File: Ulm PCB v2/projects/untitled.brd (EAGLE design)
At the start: 39.4 x 49.5 mm, 26 parts, among them U1 FT232RLSSOP, U2 MCP73831, U3 SPX3819-3.3, X2 USB-SMD-NS

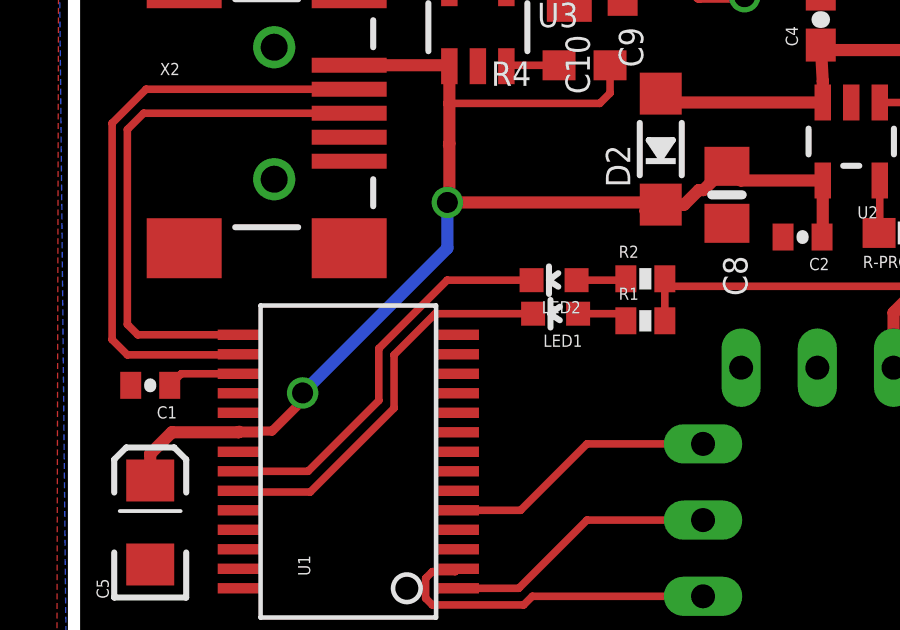
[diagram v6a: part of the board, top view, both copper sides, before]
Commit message: corrected gnd path to FT232RL
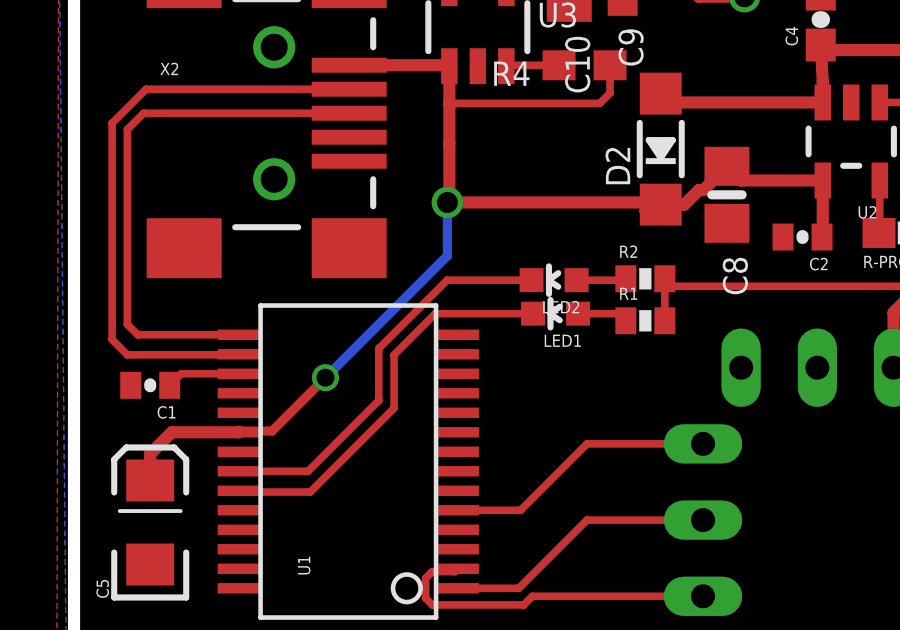
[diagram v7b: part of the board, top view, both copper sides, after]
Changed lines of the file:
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@@
 <wire x1="8.07425" y1="15.6845" x2="9.525" y2="15.9385" width="0.4064" layer="1"/>
 <wire x1="9.525" y1="15.9385" x2="9.144" y2="15.8115" width="0.4064" layer="1"/>
-<wire x1="5.488" y1="45.455" x2="5.488" y2="43.505" width="0" layer="19" extent="1-1"/>
 </signal>
 <signal name="N$9">
@@
 <wire x1="19.558" y1="51.744" x2="20.34141875" y2="51.744" width="0.4064" layer="1"/>
 <wire x1="20.34141875" y1="51.744" x2="20.82461875" y2="52.2272" width="0.4064" layer="1"/>
-<wire x1="12.446" y1="51.816" x2="12.446" y2="50.292" width="0.4064" layer="16"/>
 <wire x1="5.5068" y1="44.1738" x2="5.488" y2="44.155" width="0.4064" layer="1"/>
 <wire x1="2.54" y1="43.434" x2="2.54" y2="42.548" width="0.4064" layer="1"/>
@@
 <wire x1="3.261" y1="44.155" x2="2.54" y2="43.434" width="0.4064" layer="1"/>
 <wire x1="12.512" y1="53.782" x2="12.512" y2="51.882" width="0.4064" layer="1"/>
-<wire x1="12.512" y1="51.882" x2="12.446" y2="51.816" width="0.4064" layer="1"/>
-<wire x1="12.446" y1="51.816" x2="19.486" y2="51.816" width="0.4064" layer="1"/>
+<wire x1="19.486" y1="51.816" x2="12.446" y2="51.816" width="0.4064" layer="1"/>
 <wire x1="19.486" y1="51.816" x2="19.558" y2="51.744" width="0.4064" layer="1"/>
-<via x="7.62" y="45.466" extent="1-16" drill="0.7"/>
-<wire x1="12.446" y1="50.292" x2="7.62" y2="45.466" width="0.4064" layer="16"/>
-<wire x1="7.62" y1="45.41791875" x2="7.62" y2="45.466" width="0.4064" layer="1"/>
-<wire x1="7.62" y1="45.466" x2="7.62" y2="45.212" width="0.3048" layer="1"/>
-<wire x1="7.62" y1="45.212" x2="6.604" y2="44.196" width="0.3048" layer="1"/>
-<wire x1="6.604" y1="44.196" x2="5.529" y2="44.196" width="0.3048" layer="1"/>
+<wire x1="5.529" y1="44.196" x2="6.604" y2="44.196" width="0.3048" layer="1"/>
 <wire x1="5.529" y1="44.196" x2="5.5068" y2="44.1738" width="0.3048" layer="1"/>
+<wire x1="12.446" y1="50.038" x2="12.446" y2="51.816" width="0.3048" layer="16"/>
+<via x="8.382" y="45.974" extent="1-16" drill="0.6"/>
+<wire x1="6.604" y1="44.196" x2="8.382" y2="45.974" width="0.3048" layer="1"/>
+<wire x1="8.382" y1="45.974" x2="12.446" y2="50.038" width="0.3048" layer="16"/>
+<wire x1="12.446" y1="51.816" x2="12.512" y2="51.882" width="0" layer="19" extent="1-1"/>
 </signal>
 <signal name="SCL">

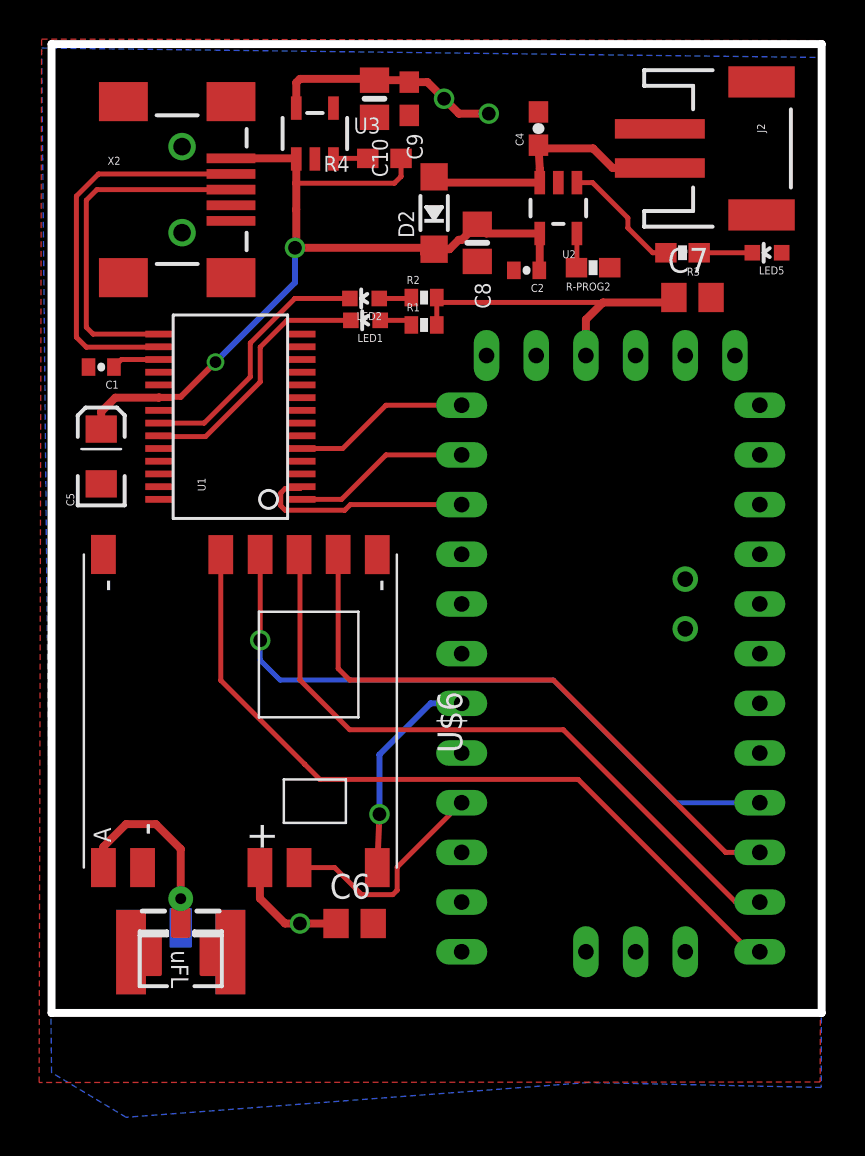
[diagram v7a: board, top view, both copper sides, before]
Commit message: corrected one polygon. made antenna trace shorter
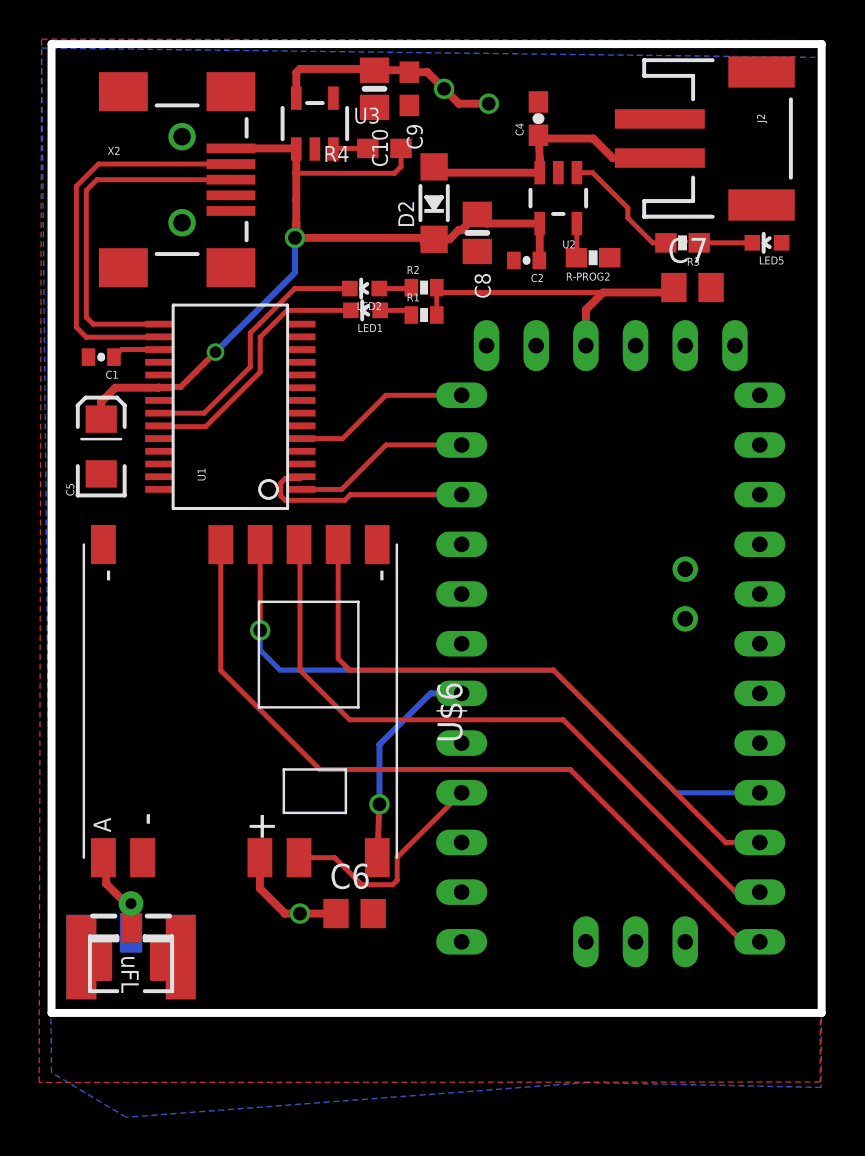
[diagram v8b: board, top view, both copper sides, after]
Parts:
- moved J$2 2.55 mm to (4.06, 13.2)
- moved C1 0.51 mm to (2.54, 46.2)
- moved C10 0.51 mm to (16.5, 59.9)
- moved C2 0.51 mm to (24.3, 51.2)
- moved C4 0.51 mm to (24.9, 58.4)
- moved C6 0.51 mm to (15.5, 17.8)
- moved C8 0.51 mm to (21.8, 52.6)
- moved C9 0.51 mm to (18.3, 59.9)
- moved J2 0.51 mm to (34.8, 57.4)
- moved LED1 0.51 mm to (16.1, 48.6)
- moved LED5 0.51 mm to (36.6, 52.1)
- moved R-PROG2 0.51 mm to (27.7, 51.3)
- moved R1 0.51 mm to (19.0, 48.4)
- moved R3 0.51 mm to (32.3, 52.1)
- moved R4 0.51 mm to (17.0, 56.9)
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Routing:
- net N$4: track 11.3 -> 5.81 mm
- net 5V: track 45.8 -> 46.6 mm
- net CS: track 39.8 -> 40.3 mm
